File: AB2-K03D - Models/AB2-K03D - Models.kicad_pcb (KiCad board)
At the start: 2 copper layers, 139 parts

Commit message: AB2-K03D: add terminal blocks and tssop
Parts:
- added AB2_TB_02_RA_5.08MM_L-BLK: VAL**, AB2_TB_02_RA_5.08MM_L-BLK, F.Cu at (174.0, 280.7)
- added AB2_TB_02_RA_5.08MM_L-BLU: VAL**, AB2_TB_02_RA_5.08MM_L-BLU, F.Cu at (174.0, 269.2)
- added AB2_TB_02_RA_5.08MM_L-GRN: VAL**, AB2_TB_02_RA_5.08MM_L-GRN, F.Cu at (174.0, 257.8)
- added AB2_TB_02_RA_5.08MM_R-BLK: VAL**, AB2_TB_02_RA_5.08MM_R-BLK, F.Cu at (185.4, 280.7)
- added AB2_TB_02_RA_5.08MM_R-BLU: VAL**, AB2_TB_02_RA_5.08MM_R-BLU, F.Cu at (185.4, 269.2)
- added AB2_TB_02_RA_5.08MM_R-GRN: VAL**, AB2_TB_02_RA_5.08MM_R-GRN, F.Cu at (185.4, 257.8)
- added AB2_TB_02_RA_5MM_L-BLK: VAL**, AB2_TB_02_RA_5MM_L-BLK, F.Cu at (196.8, 280.7)
- added AB2_TB_02_RA_5MM_L-BLU: VAL**, AB2_TB_02_RA_5MM_L-BLU, F.Cu at (196.8, 269.2)
- added AB2_TB_02_RA_5MM_L-GRN: VAL**, AB2_TB_02_RA_5MM_L-GRN, F.Cu at (196.8, 257.8)
- added AB2_TB_02_RA_5MM_R-BLK: VAL**, AB2_TB_02_RA_5MM_R-BLK, F.Cu at (208.3, 280.7)
- added AB2_TB_02_RA_5MM_R-BLU: VAL**, AB2_TB_02_RA_5MM_R-BLU, F.Cu at (208.3, 269.2)
- added AB2_TB_02_RA_5MM_R-GRN: VAL**, AB2_TB_02_RA_5MM_R-GRN, F.Cu at (208.3, 257.8)
- added AB2_TB_04_RA_5.08MM_L-BLK: VAL**, AB2_TB_04_RA_5.08MM_L-BLK, F.Cu at (224.8, 280.7)
- added AB2_TB_04_RA_5.08MM_L-BLU: VAL**, AB2_TB_04_RA_5.08MM_L-BLU, F.Cu at (224.8, 269.2)
- added AB2_TB_04_RA_5.08MM_L-GRN: VAL**, AB2_TB_04_RA_5.08MM_L-GRN, F.Cu at (224.8, 257.8)
- added AB2_TB_04_RA_5.08MM_R-BLK: VAL**, AB2_TB_04_RA_5.08MM_R-BLK, F.Cu at (246.4, 280.7)
- added AB2_TB_04_RA_5.08MM_R-BLU: VAL**, AB2_TB_04_RA_5.08MM_R-BLU, F.Cu at (246.4, 269.2)
- added AB2_TB_04_RA_5.08MM_R-GRN: VAL**, AB2_TB_04_RA_5.08MM_R-GRN, F.Cu at (246.4, 257.8)
- added AB2_TB_04_RA_5MM_L-BLK: VAL**, AB2_TB_04_RA_5MM_L-BLK, F.Cu at (268.0, 280.7)
- added AB2_TB_04_RA_5MM_L-BLU: VAL**, AB2_TB_04_RA_5MM_L-BLU, F.Cu at (268.0, 269.2)
- added AB2_TB_04_RA_5MM_L-GRN: VAL**, AB2_TB_04_RA_5MM_L-GRN, F.Cu at (268.0, 257.8)
- added AB2_TB_04_RA_5MM_R-BLK: VAL**, AB2_TB_04_RA_5MM_R-BLK, F.Cu at (289.6, 280.7)
- added AB2_TB_04_RA_5MM_R-BLU: VAL**, AB2_TB_04_RA_5MM_R-BLU, F.Cu at (289.6, 269.2)
- added AB2_TB_04_RA_5MM_R-GRN: VAL**, AB2_TB_04_RA_5MM_R-GRN, F.Cu at (289.6, 257.8)
- added AB2_TSSOP08: VAL**, AB2_TSSOP08, F.Cu at (16.5, 242.6)
- added AB2_TSSOP14: VAL**, AB2_TSSOP14, F.Cu at (21.6, 242.6)
- added AB2_TSSOP16: VAL**, AB2_TSSOP16, F.Cu at (27.9, 242.6)
- added AB2_TSSOP20: VAL**, AB2_TSSOP20, F.Cu at (34.3, 242.6)
- added AB2_TSSOP24: VAL**, AB2_TSSOP24, F.Cu at (41.9, 242.6)
- added AB2_TSSOP28: VAL**, AB2_TSSOP28, F.Cu at (52.1, 242.6)
- added AB2_TSSOP28_PWP: VAL**, AB2_TSSOP28_PWP, F.Cu at (63.5, 242.6)
- added AB2_TSSOP28_PWP_SLUG: VAL**, AB2_TSSOP28_PWP_SLUG, F.Cu at (74.9, 242.6)
- moved AB2_HDR_M01-1V 277.9 mm to (234.9, 185.4), turned to 270 degrees
- moved AB2_HDR_M01-1H-L 275.4 mm to (287.0, 118.1), turned to 270 degrees
- moved AB2_HDR_M02-1V 274.1 mm to (232.4, 186.7), turned to 270 degrees
- moved AB2_HDR_M02-1H-L 271.8 mm to (284.5, 119.4), turned to 270 degrees
- moved AB2_HDR_M03-1V 270.3 mm to (229.9, 188.0), turned to 270 degrees
- moved AB2_HDR_M03-1H-L 268.3 mm to (281.9, 120.7), turned to 270 degrees
- moved AB2_HDR_M04-1V 266.6 mm to (227.3, 189.2), turned to 270 degrees
- moved AB2_HDR_M04-1H-L 264.8 mm to (279.4, 121.9), turned to 270 degrees
- moved AB2_HDR_M05-1V 262.8 mm to (224.8, 190.5), turned to 270 degrees
- moved AB2_HDR_M05-1H-L 261.3 mm to (276.9, 123.2), turned to 270 degrees
- moved HDR1 259.0 mm to (222.2, 191.8), turned to 270 degrees
- moved AB2_HDR_M06-1H-L 257.8 mm to (274.3, 124.5), turned to 270 degrees
- moved AB2_HDR_M07-1V 255.3 mm to (219.7, 193.0), turned to 270 degrees
- moved AB2_HDR_M07-1H-L 254.3 mm to (271.8, 125.7), turned to 270 degrees
- moved AB2_HDR_M25-1H-R 252.7 mm to (298.4, 148.6), turned to 90 degrees
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
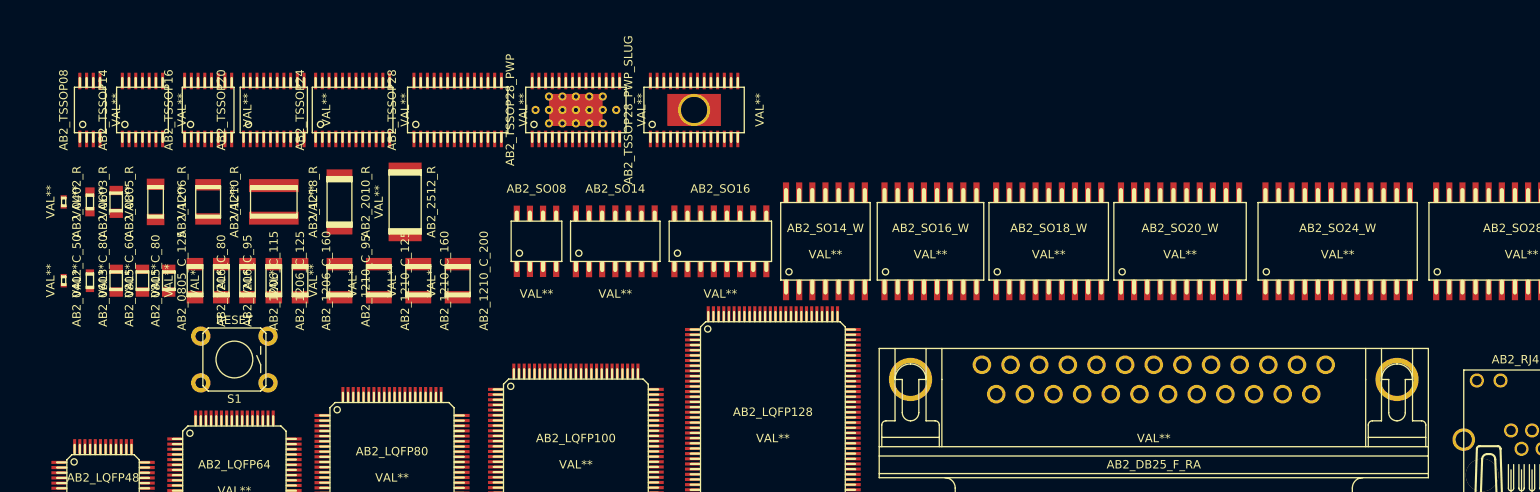
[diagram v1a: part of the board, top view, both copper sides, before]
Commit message: AB2-K03D: add pwr barrel and tssop packages
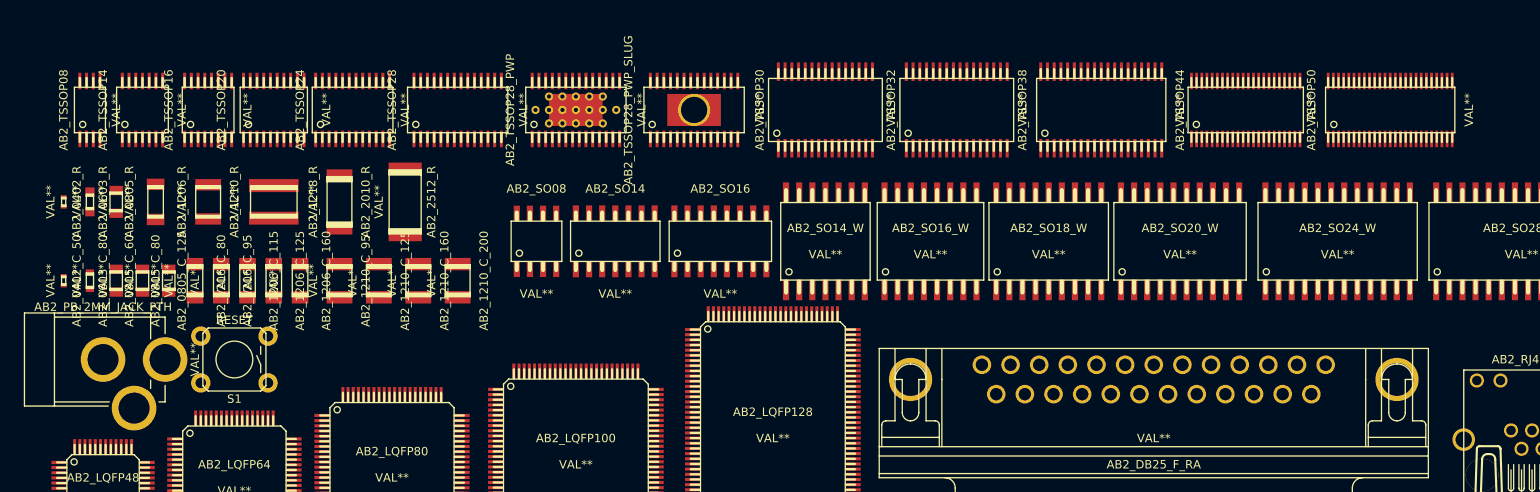
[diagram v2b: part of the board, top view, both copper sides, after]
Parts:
- added AB2_PB_2MM_JACK_PTH: VAL**, AB2_PB_2MM_JACK_PTH, F.Cu at (17.8, 266.7)
- added AB2_TSSOP30: VAL**, AB2_TSSOP30, F.Cu at (87.6, 242.6)
- added AB2_TSSOP32: VAL**, AB2_TSSOP32, F.Cu at (100.3, 242.6)
- added AB2_TSSOP38: VAL**, AB2_TSSOP38, F.Cu at (114.3, 242.6)
- added AB2_TSSOP44: VAL**, AB2_TSSOP44, F.Cu at (128.3, 242.6)
- added AB2_TSSOP50: VAL**, AB2_TSSOP50, F.Cu at (142.2, 242.6)

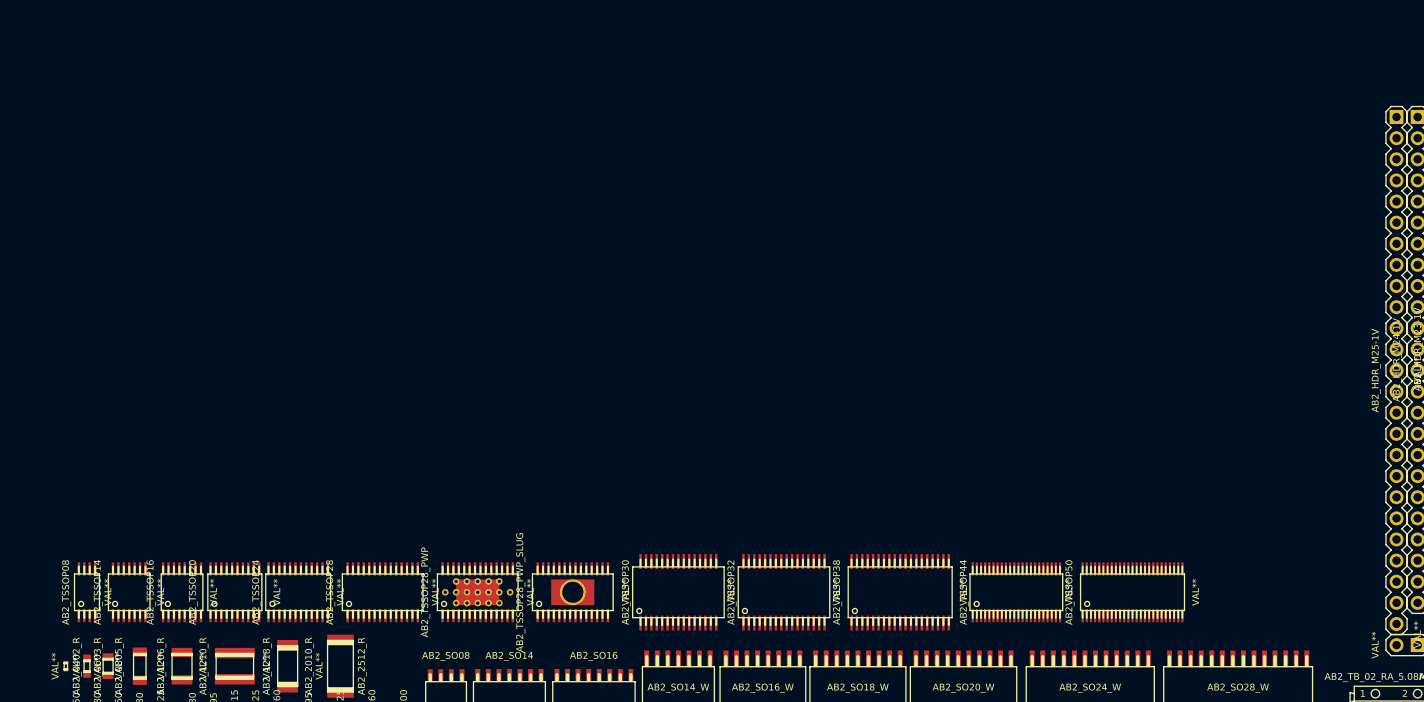
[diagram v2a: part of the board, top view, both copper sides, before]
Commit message: AB2-K03D: add usb and 7 segments
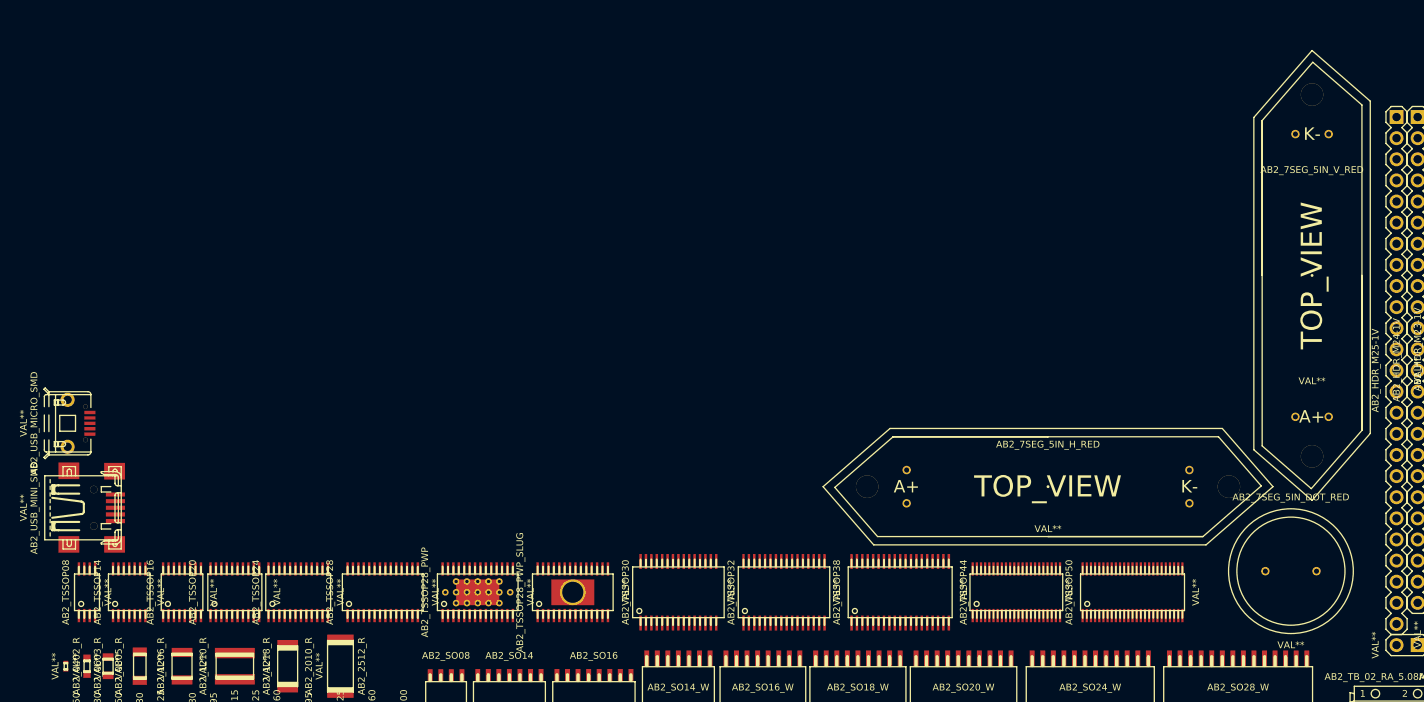
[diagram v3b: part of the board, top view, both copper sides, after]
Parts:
- added AB2_7SEG_5IN_DOT_RED: VAL**, AB2_7SEG_5IN_DOT_RED, F.Cu at (161.3, 240.0)
- added AB2_7SEG_5IN_H_RED: VAL**, AB2_7SEG_5IN_H_RED, F.Cu at (132.1, 229.9)
- added AB2_7SEG_5IN_V_RED: VAL**, AB2_7SEG_5IN_V_RED, F.Cu at (163.8, 204.5)
- added AB2_USB_MICRO_SMD: VAL**, AB2_USB_MICRO_SMD, F.Cu at (11.4, 222.2)
- added AB2_USB_MINI_SMD: VAL**, AB2_USB_MINI_SMD, F.Cu at (11.4, 232.4)
